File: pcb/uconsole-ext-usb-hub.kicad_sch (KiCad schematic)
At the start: 35 parts, among them J1 MINI_PCIE, J2 SPEAKER, J3 SPEAKER, P1 USB_C_Plug_USB2.0, P2 USB_C_Plug_USB2.0, P3 USB_C_Plug_USB2.0, P4 USB_C_Plug_USB2.0, U1 TUSB2048B, U2 TPS2044D, U3 USBLC6-2P6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

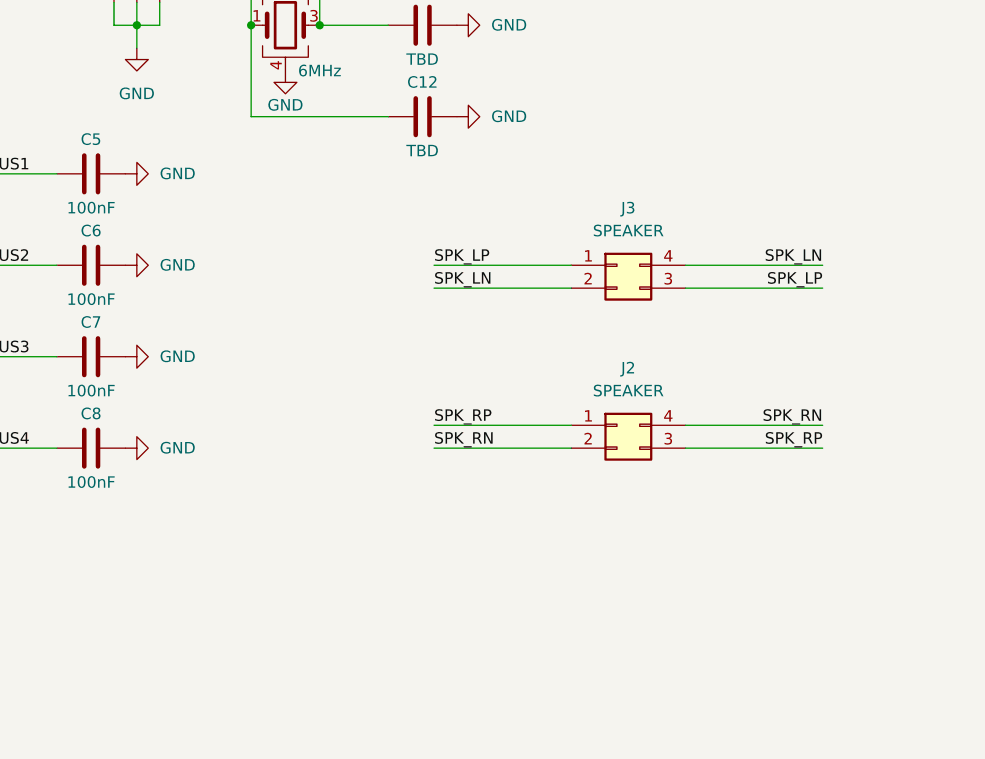
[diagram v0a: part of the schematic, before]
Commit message: Some updates of sch, pcb and readme
* Add 3 u.fl connectors for antennas
* Update pictures in readme

Signed-off-by: argz <kirill.snezhko@pm.me>
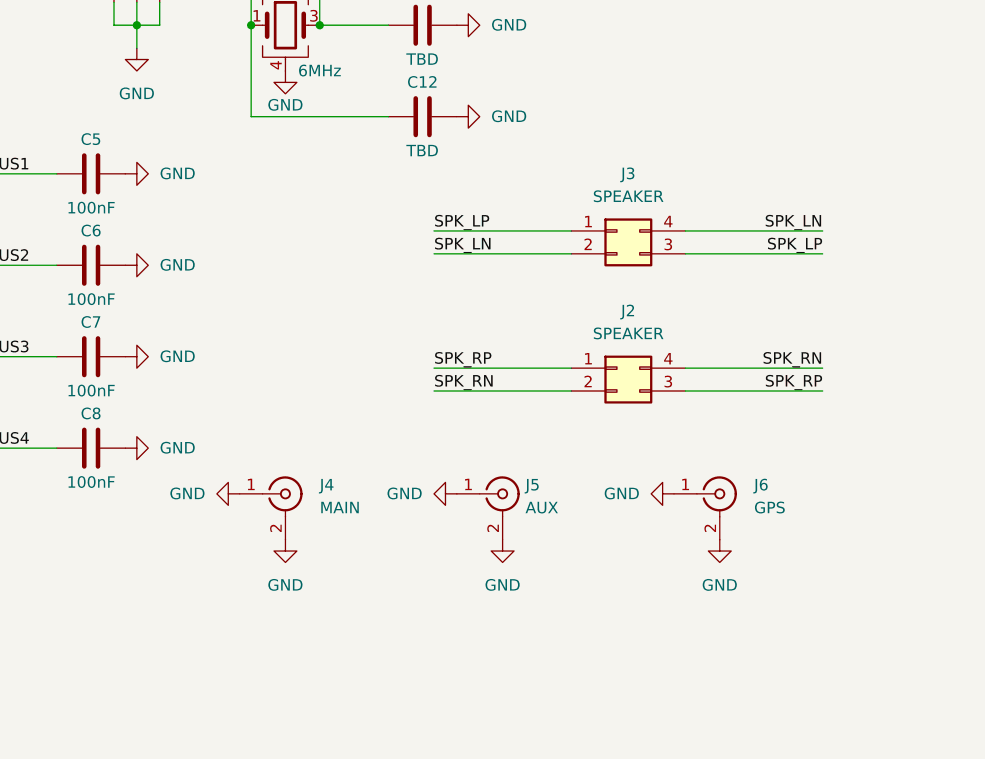
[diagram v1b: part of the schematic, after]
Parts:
- added J4: MAIN, Connector_Coaxial:U.FL_Hirose_U.FL-R-SMT-1_Vertical, symbol Connector:Conn_Coaxial
- added J5: AUX, Connector_Coaxial:U.FL_Hirose_U.FL-R-SMT-1_Vertical, symbol Connector:Conn_Coaxial
- added J6: GPS, Connector_Coaxial:U.FL_Hirose_U.FL-R-SMT-1_Vertical, symbol Connector:Conn_Coaxial
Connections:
- net GND: now also J4.1 (In), J4.2 (Ext), J5.1 (In), J5.2 (Ext), J6.1 (In), J6.2 (Ext)
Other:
- moved on the sheet: J2, J3
